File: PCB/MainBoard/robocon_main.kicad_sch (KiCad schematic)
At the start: 29 parts, among them J1 MOTOR_OUT, J10 Conn_01x03_Pin, J11 to_SERVO, J2 Conn_01x02_Pin, J3 MOTOR_OUT, J4 Conn_01x02_Pin, J5 MOTOR_OUT, J6 Conn_01x02_Pin, J7 MOTOR_OUT, J8 Conn_01x02_Pin, J9 to_CAM, M1 Motor_DC, M2 Motor_DC, M3 Motor_DC, M4 Motor_DC, SW1 POW, U1 OKL-T/6-W12N-C, U2 RP2040, U3 TB67H450, U4 3-Terminal Regulator, U5 TB67H450, U6 TB67H450, U7 TB67H450, U8 BNO055, U9 UnitV-M12

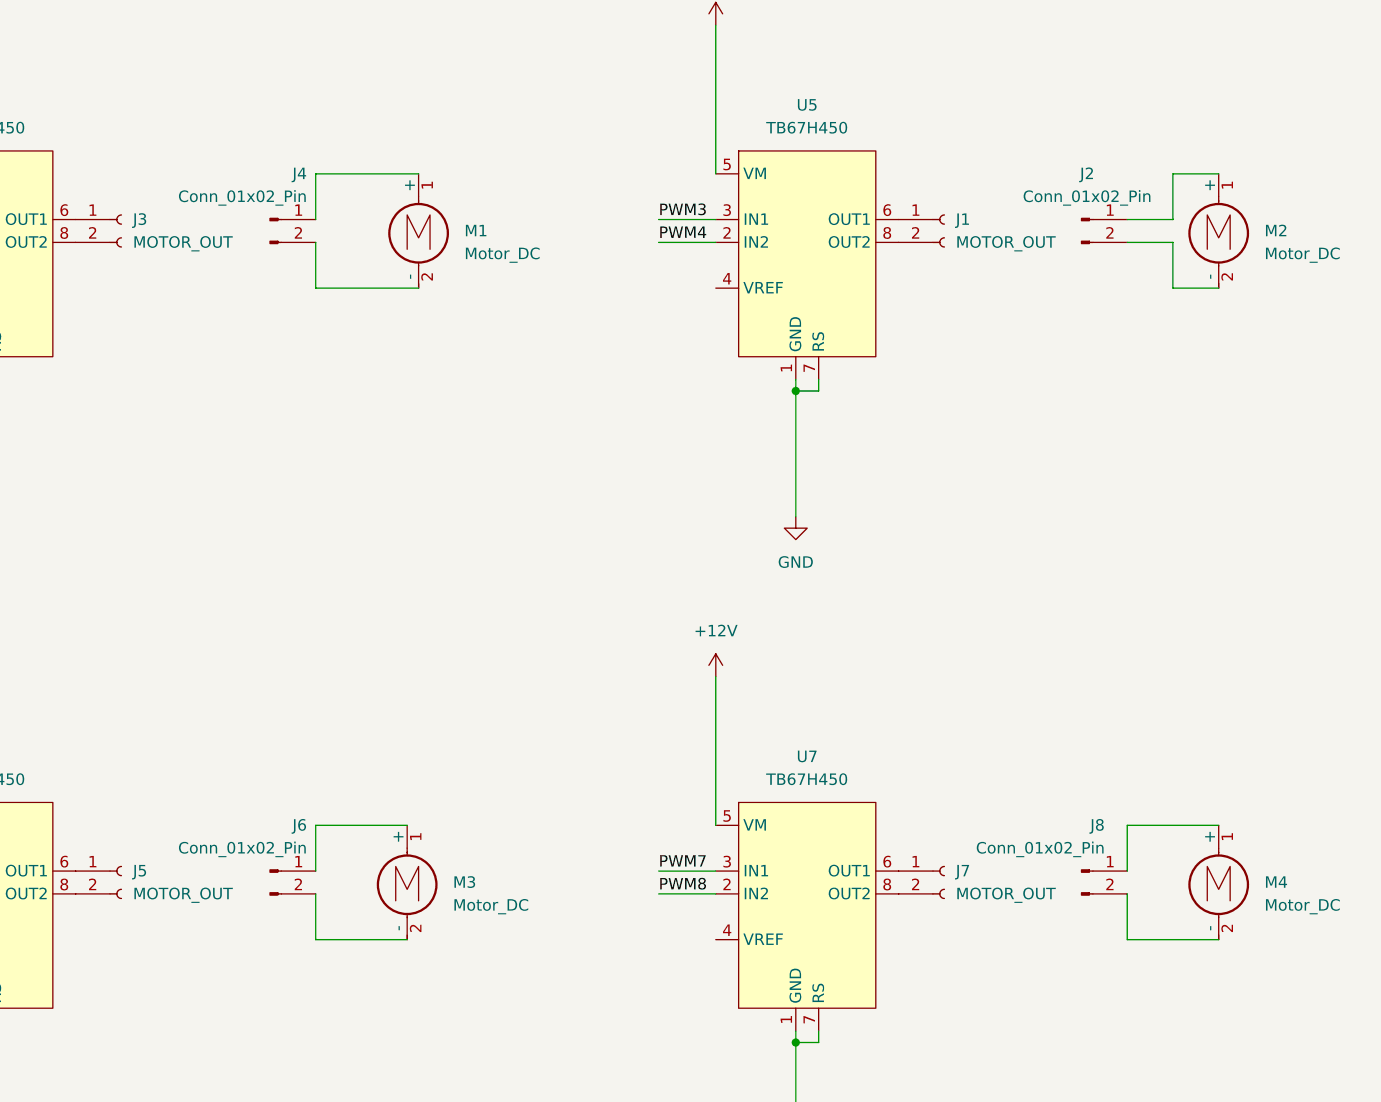
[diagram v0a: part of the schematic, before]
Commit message: モータのシンボル削除
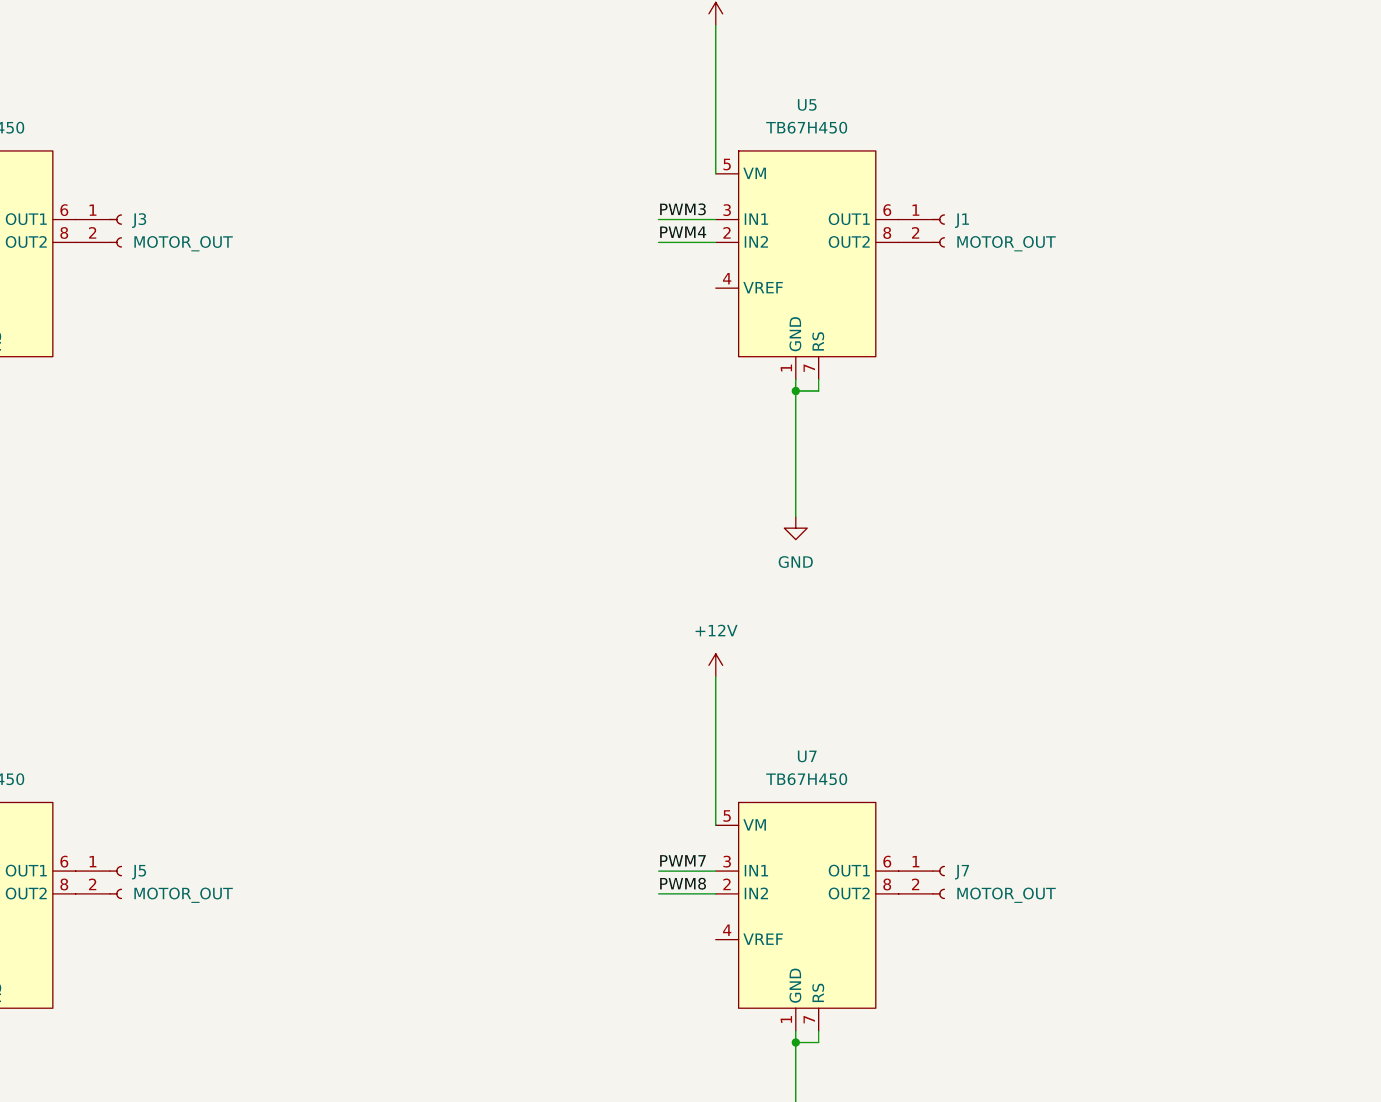
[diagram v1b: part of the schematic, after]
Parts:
- removed J2, J4, J6, J8: Conn_01x02_Pin, symbol Connector:Conn_01x02_Pin
- removed M1, M2, M3, M4: Motor_DC, symbol Motor:Motor_DC

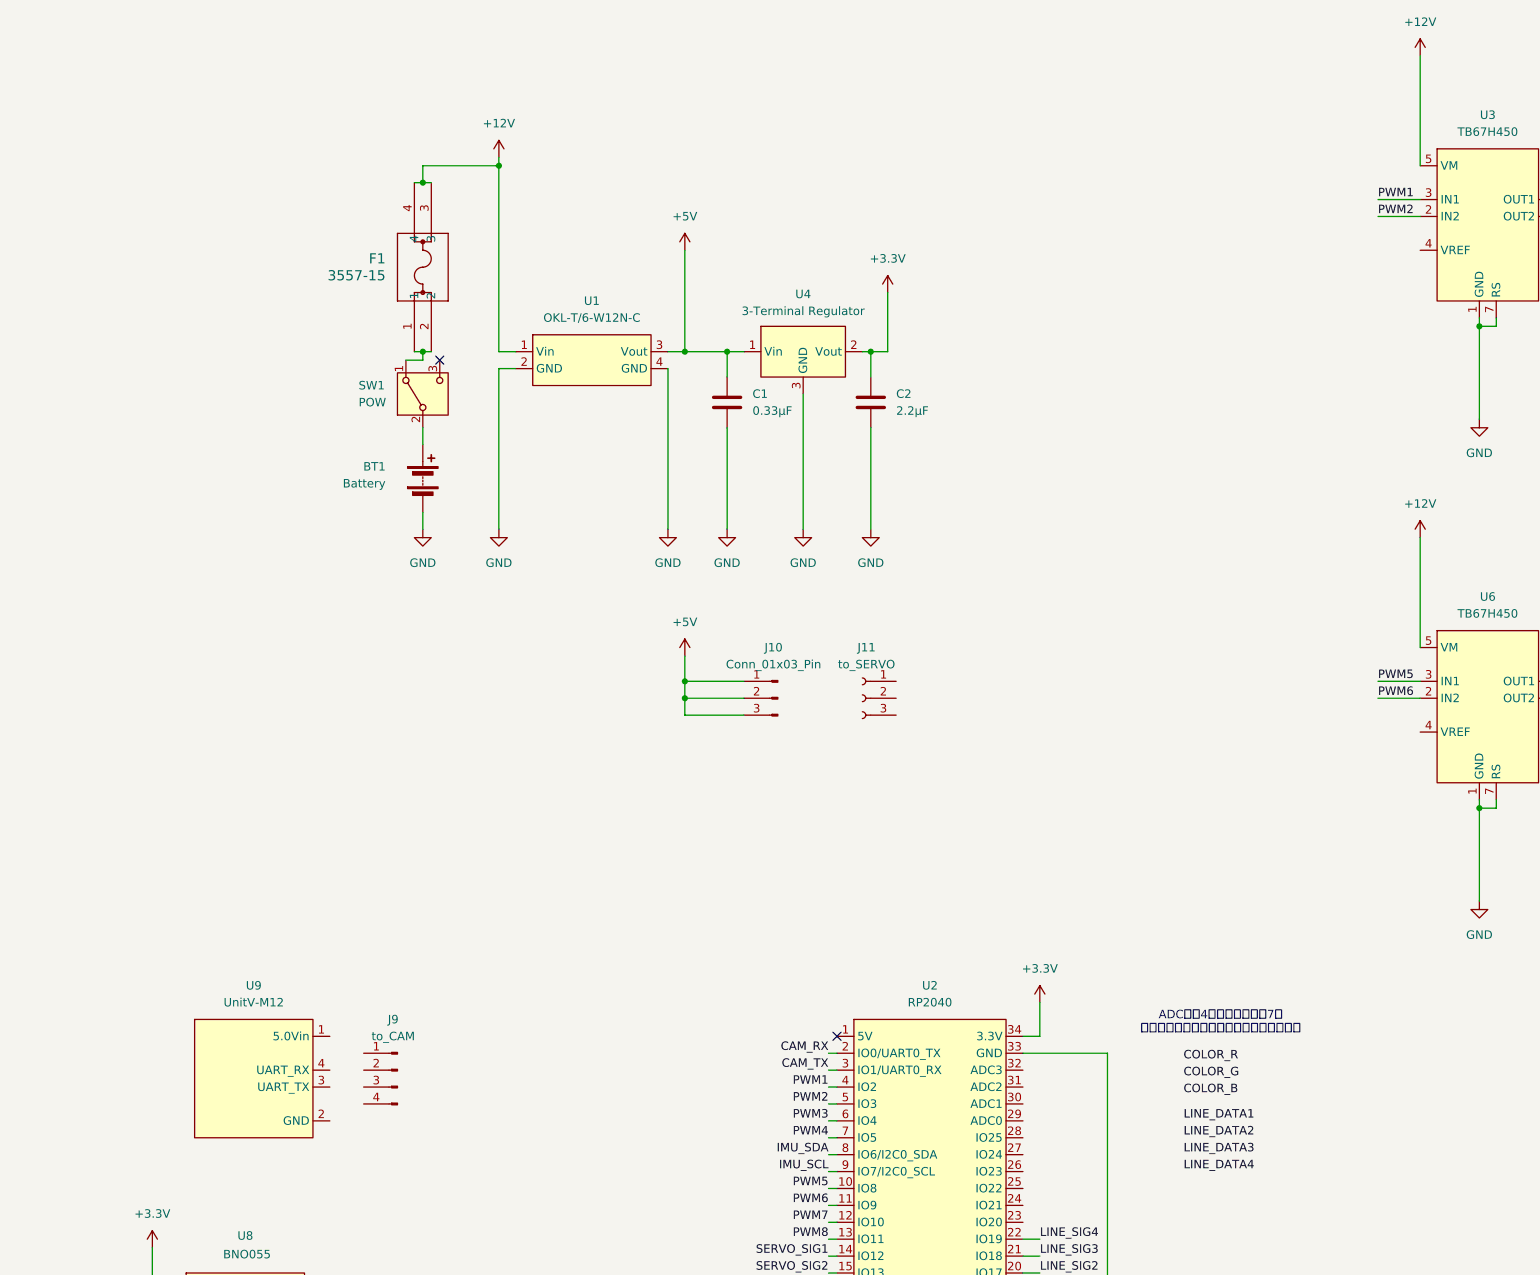
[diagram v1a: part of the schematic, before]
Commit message: カメラのコネクタ配線
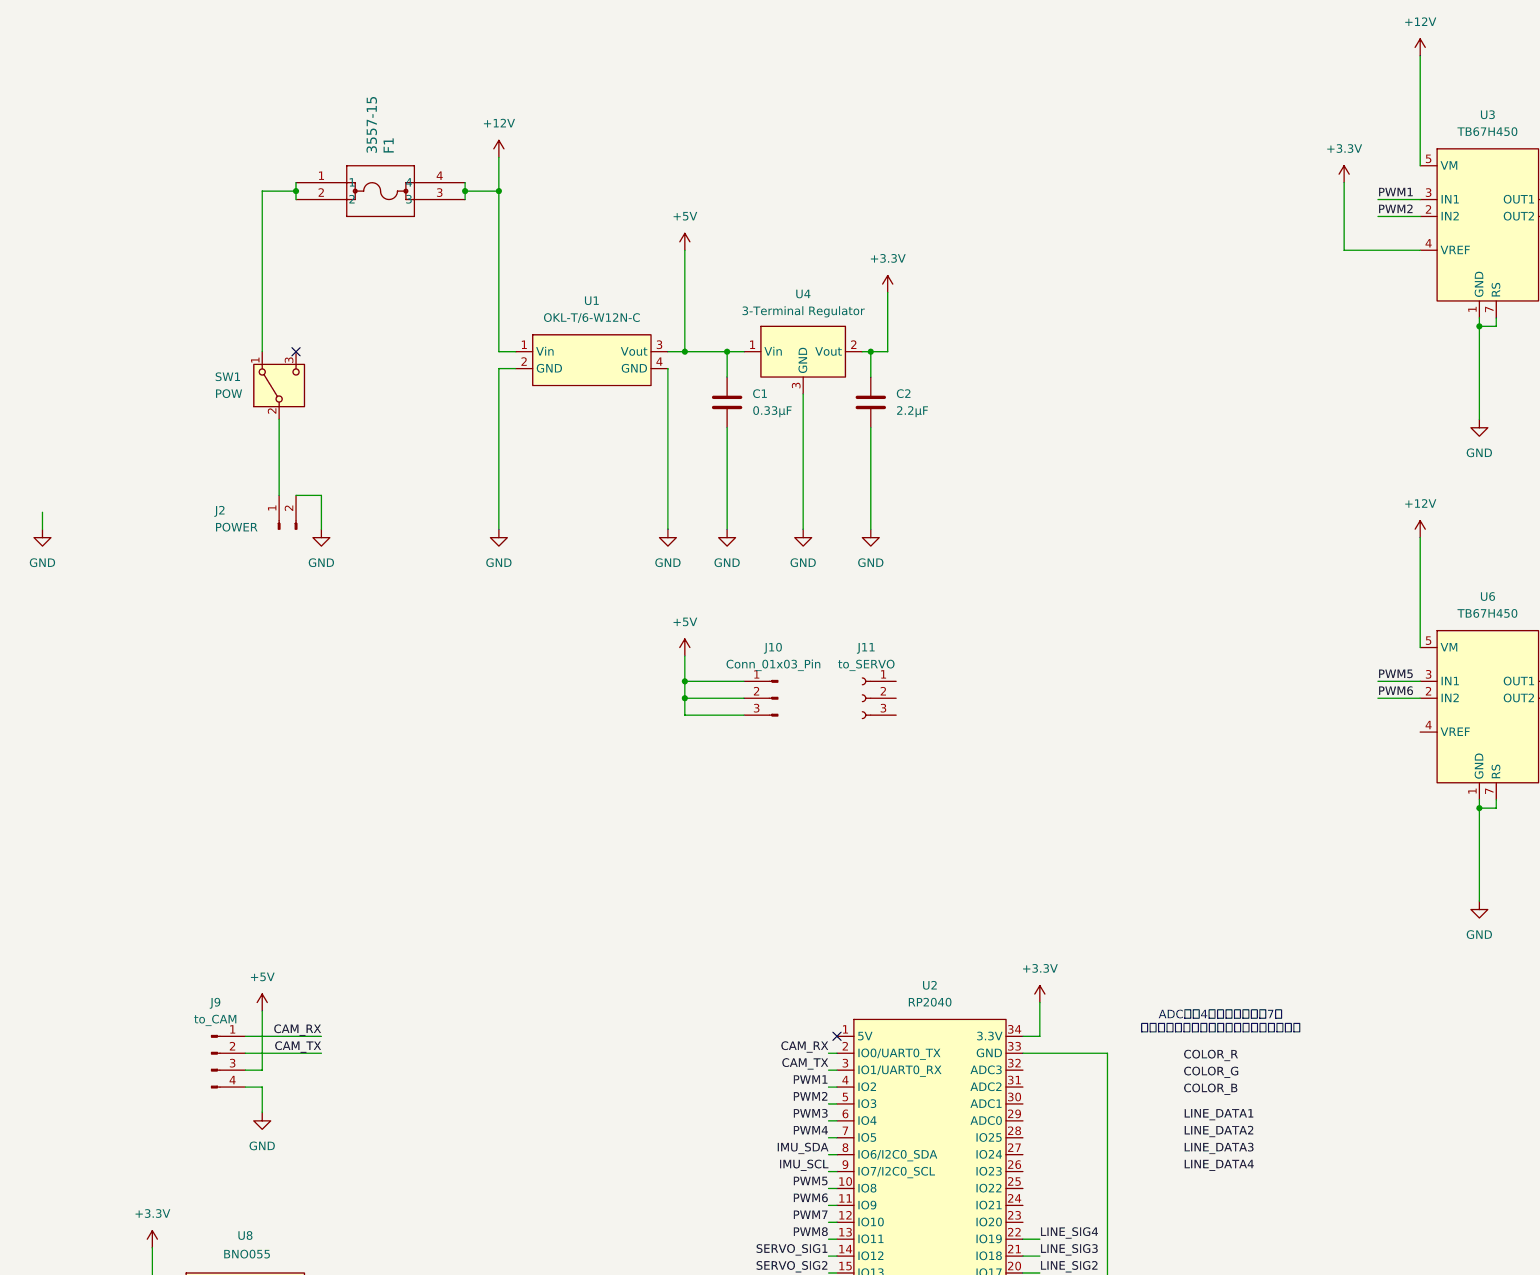
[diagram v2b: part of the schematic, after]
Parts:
- removed BT1: Battery, symbol Device:Battery
- removed U9: UnitV-M12, symbol my_symbol:UnitV-M12
- added J2: POWER, symbol Connector:Conn_01x02_Pin
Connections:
- net +3.3V: now also U3.4 (VREF)
- net +5V: now also J9.3 (Pin_3)
- net CAM_RX: now also J9.1 (Pin_1)
- net CAM_TX: now also J9.2 (Pin_2)
- net GND: now also J9.4 (Pin_4), J2.2 (Pin_2)
- net at SW1.2 (B): now also J2.1 (Pin_1)
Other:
- moved on the sheet: F1, J9, SW1

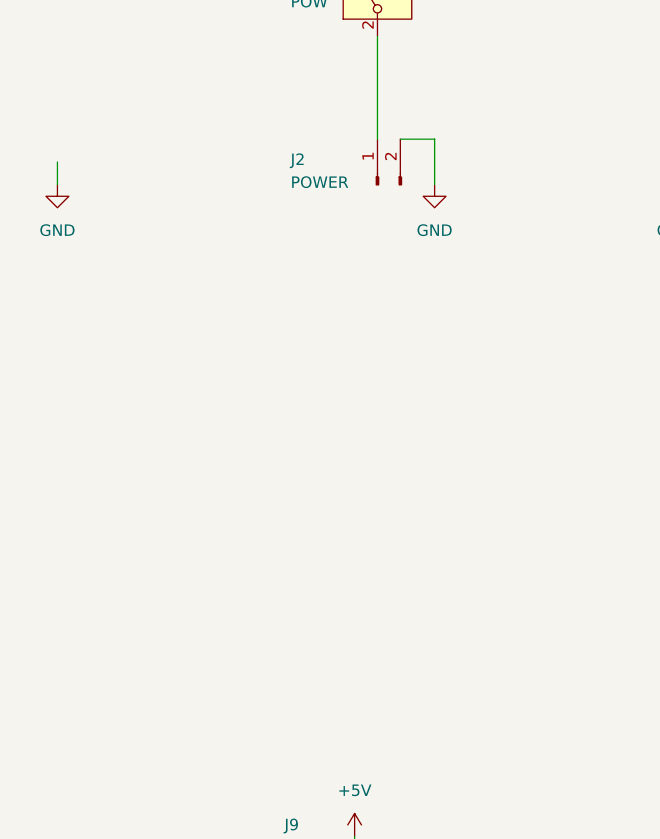
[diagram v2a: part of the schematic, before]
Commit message: フットプリントの割り当てなど_ver.1
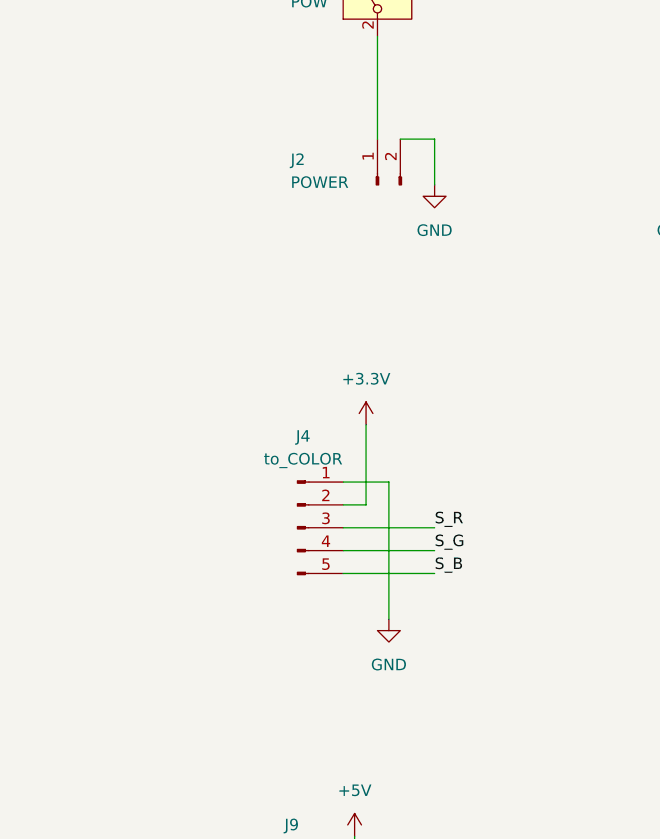
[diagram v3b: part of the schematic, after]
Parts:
- added J4: to_COLOR, Connector_JST:JST_PH_B5B-PH-K_1x05_P2.00mm_Vertical, symbol Connector:Conn_01x05_Pin
- U2: footprint (none) -> RP2040:RP2040
- U3, U5, U6, U7: footprint (none) -> my_footprints_library:AE-TB67H450
- U8: footprint (none) -> my_footprints_library:BNO055
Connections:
- net +3.3V: now also J4.2 (Pin_2)
- net GND: now also J4.1 (Pin_1)
- new net S_B: J4.5 (Pin_5)
- new net S_G: J4.4 (Pin_4)
- new net S_R: J4.3 (Pin_3)
